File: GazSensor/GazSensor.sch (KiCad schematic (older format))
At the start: 19 parts, among them P1 Power, P2 Analog, P3 Digital, P4 Digital, P5 CONN_01X01, P6 CONN_01X01, P7 CONN_01X01, P8 CONN_01X01, U101 RN2483_breakout, U102 LTC1050

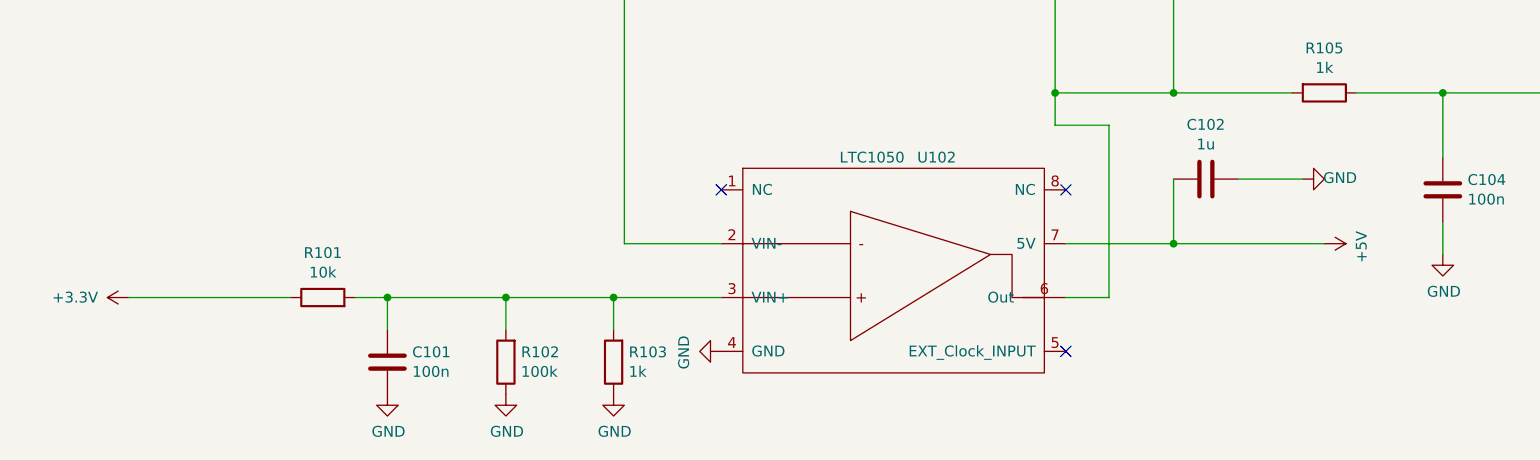
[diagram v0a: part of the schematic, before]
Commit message: Sheild PCB
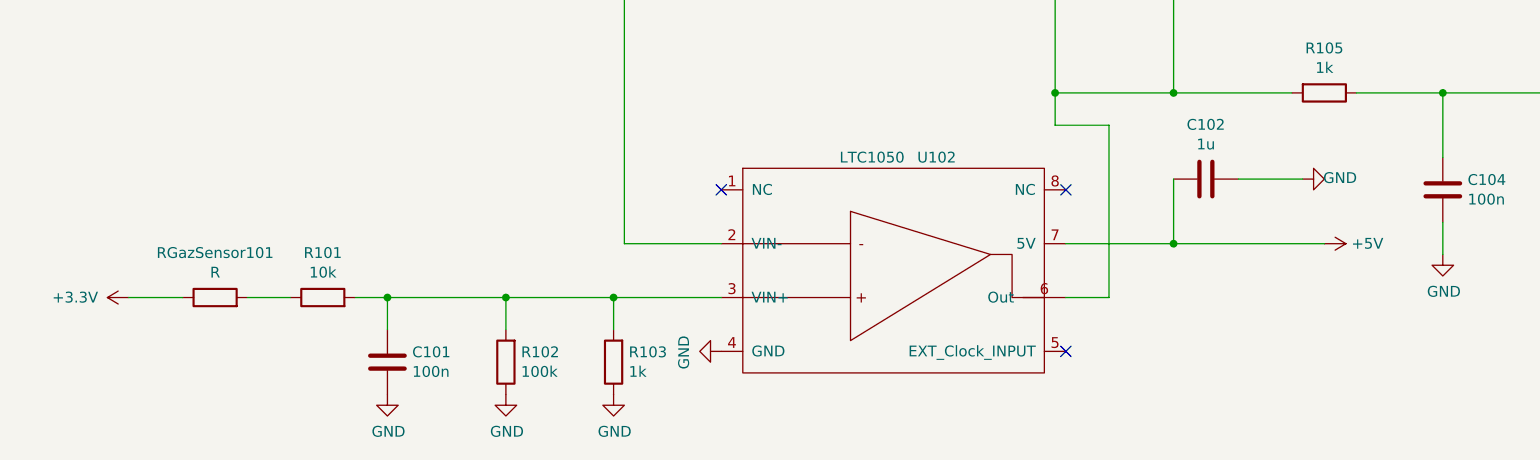
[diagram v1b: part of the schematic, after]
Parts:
- added RGazSensor101: R, MyComponents:GazSensor, symbol Device:R
- C101, C102, C103, C104: footprint Capacitors_SMD:CP_Elec_3x5.3 -> Capacitor_THT:CP_Radial_D4.0mm_P1.50mm
- R101, R102, R103, R104, R105: footprint Resistors_SMD:R_0201_0603Metric -> Resistor_THT:R_Axial_DIN0207_L6.3mm_D2.5mm_P7.62mm_Horizontal
- U101: footprint Connector_Pin:Pin_D0.7mm_L6.5mm_W1.8mm_FlatFork -> MyComponents:RN2483_Breakout
- U102: footprint Connector_Pin:Pin_D0.7mm_L6.5mm_W1.8mm_FlatFork -> MyComponents:PDIP-8_N
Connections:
- net +3V3: now also RGazSensor101.1; no longer R101.1
- new net: R101.1, RGazSensor101.2
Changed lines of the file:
@@
 encoding utf-8
 Sheet 1 1
-Title ""
+Title "GAZ Sensor qheild"
 Date "lun. 30 mars 2015"
 Rev ""
-Comp ""
-Comment1 ""
-Comment2 ""
-Comment3 ""
+Comp "INSA of Toulouse"
+Comment1 "Vincent Laurens"
+Comment2 "Mickaël Commérot"
+Comment3 "Hamza Safri"
 Comment4 ""
 $EndDescr
@@
 P 6900 4800
 F 0 "#PWR0107" H 6900 4650 50  0001 C CNN
-F 1 "+5V" H 6915 4973 50  0000 C CNN
+F 1 "+5V" V 6900 5000 50  0000 C CNN
 F 2 "" H 6900 4800 50  0001 C CNN
 F 3 "" H 6900 4800 50  0001 C CNN
@@
 F 0 "U101" H 5378 615 50  0000 L CNN
 F 1 "RN2483_breakout" H 5378 524 50  0000 L CNN
-F 2 "Connector_Pin:Pin_D0.7mm_L6.5mm_W1.8mm_FlatFork" H 4800 950 50  0001 C CNN
+F 2 "MyComponents:RN2483_Breakout" H 4800 950 50  0001 C CNN
 F 3 "" H 4800 950 50  0001 C CNN
 	1    4800 950
@@
 F 0 "R105" V 6693 4100 50  0000 C CNN
 F 1 "1k" V 6784 4100 50  0000 C CNN
-F 2 "Resistors_SMD:R_0201_0603Metric" V 6830 4100 50  0001 C CNN
+F 2 "Resistor_THT:R_Axial_DIN0207_L6.3mm_D2.5mm_P7.62mm_Horizontal" V 6830 4100 50  0001 C CNN
 F 3 "~" H 6900 4100 50  0001 C CNN
 	1    6900 4100
@@
 F 0 "C104" H 7565 4596 50  0000 L CNN
 F 1 "100n" H 7565 4505 50  0000 L CNN
-F 2 "Capacitors_SMD:CP_Elec_3x5.3" H 7488 4400 50  0001 C CNN
+F 2 "Capacitor_THT:CP_Radial_D4.0mm_P1.50mm" H 7488 4400 50  0001 C CNN
 F 3 "~" H 7450 4550 50  0001 C CNN
 	1    7450 4550
@@
 F 0 "R104" H 5580 3404 50  0000 R CNN
 F 1 "100k" H 5580 3495 50  0000 R CNN
-F 2 "Resistors_SMD:R_0201_0603Metric" V 5580 3450 50  0001 C CNN
+F 2 "Resistor_THT:R_Axial_DIN0207_L6.3mm_D2.5mm_P7.62mm_Horizontal" V 5580 3450 50  0001 C CNN
 F 3 "~" H 5650 3450 50  0001 C CNN
 	1    5650 3450
@@
 F 0 "C102" V 6098 4500 50  0000 C CNN
 F 1 "1u" V 6189 4500 50  0000 C CNN
-F 2 "Capacitors_SMD:CP_Elec_3x5.3" H 6388 4350 50  0001 C CNN
+F 2 "Capacitor_THT:CP_Radial_D4.0mm_P1.50mm" H 6388 4350 50  0001 C CNN
 F 3 "~" H 6350 4500 50  0001 C CNN
 	1    6350 4500
@@
 F 0 "C103" H 6315 3546 50  0000 L CNN
 F 1 "100n" H 6315 3455 50  0000 L CNN
-F 2 "Capacitors_SMD:CP_Elec_3x5.3" H 6238 3350 50  0001 C CNN
+F 2 "Capacitor_THT:CP_Radial_D4.0mm_P1.50mm" H 6238 3350 50  0001 C CNN
 F 3 "~" H 6200 3500 50  0001 C CNN
 	1    6200 3500
@@
 F 0 "R103" H 3530 5304 50  0000 R CNN
 F 1 "1k" H 3530 5395 50  0000 R CNN
-F 2 "Resistors_SMD:R_0201_0603Metric" V 3530 5350 50  0001 C CNN
+F 2 "Resistor_THT:R_Axial_DIN0207_L6.3mm_D2.5mm_P7.62mm_Horizontal" V 3530 5350 50  0001 C CNN
 F 3 "~" H 3600 5350 50  0001 C CNN
 	1    3600 5350
@@
 F 0 "C101" H 2665 5396 50  0000 L CNN
 F 1 "100n" H 2665 5305 50  0000 L CNN
-F 2 "Capacitors_SMD:CP_Elec_3x5.3" H 2588 5200 50  0001 C CNN
+F 2 "Capacitor_THT:CP_Radial_D4.0mm_P1.50mm" H 2588 5200 50  0001 C CNN
 F 3 "~" H 2550 5350 50  0001 C CNN
 	1    2550 5350
@@
 F 0 "R102" H 3030 5304 50  0000 R CNN
 F 1 "100k" H 3030 5395 50  0000 R CNN
-F 2 "Resistors_SMD:R_0201_0603Metric" V 3030 5350 50  0001 C CNN
+F 2 "Resistor_THT:R_Axial_DIN0207_L6.3mm_D2.5mm_P7.62mm_Horizontal" V 3030 5350 50  0001 C CNN
 F 3 "~" H 3100 5350 50  0001 C CNN
 	1    3100 5350
@@
 F 0 "R101" V 2457 5050 50  0000 C CNN
 F 1 "10k" V 2366 5050 50  0000 C CNN
-F 2 "Resistors_SMD:R_0201_0603Metric" V 2180 5050 50  0001 C CNN
+F 2 "Resistor_THT:R_Axial_DIN0207_L6.3mm_D2.5mm_P7.62mm_Horizontal" V 2180 5050 50  0001 C CNN
 F 3 "~" H 2250 5050 50  0001 C CNN
 	1    2250 5050
@@
 	5650 2500 6200 2500
 Wire Wire Line
-	2100 5050 1350 5050
+	2100 5050 1900 5050
 $Comp
 L power:PWR_FLAG #FLG0103
@@
 F 0 "U102" H 5100 3900 50  0000 C CNN
 F 1 "LTC1050" H 4800 3900 50  0000 C CNN
-F 2 "Connector_Pin:Pin_D0.7mm_L6.5mm_W1.8mm_FlatFork" H 5200 4150 50  0001 C CNN
+F 2 "MyComponents:PDIP-8_N" H 5200 4150 50  0001 C CNN
 F 3 "" H 5200 4150 50  0001 C CNN
 	1    5200 4150
@@
 	5650 4250 5650 4100
 Connection ~ 5650 4100
+$Comp
+L Device:R RGazSensor101
+U 1 1 5DFFA45E
+P 1750 5050
+F 0 "RGazSensor101" V 1957 5050 50  0000 C CNN
+F 1 "R" V 1866 5050 50  0000 C CNN
+F 2 "MyComponents:GazSensor" V 1680 5050 50  0001 C CNN
+F 3 "~" H 1750 5050 50  0001 C CNN
+	1    1750 5050
+	0    -1   -1   0
+$EndComp
+Wire Wire Line
+	1600 5050 1350 5050
 $EndSCHEMATC
